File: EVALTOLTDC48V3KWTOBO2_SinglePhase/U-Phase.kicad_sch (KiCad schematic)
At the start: 35 parts, among them Q1 IAUS300N10S5N015TATMA1, Q4 IAUS300N10S5N015TATMA1, U3 2EDL8x24G, U4 NL27WZ08USG

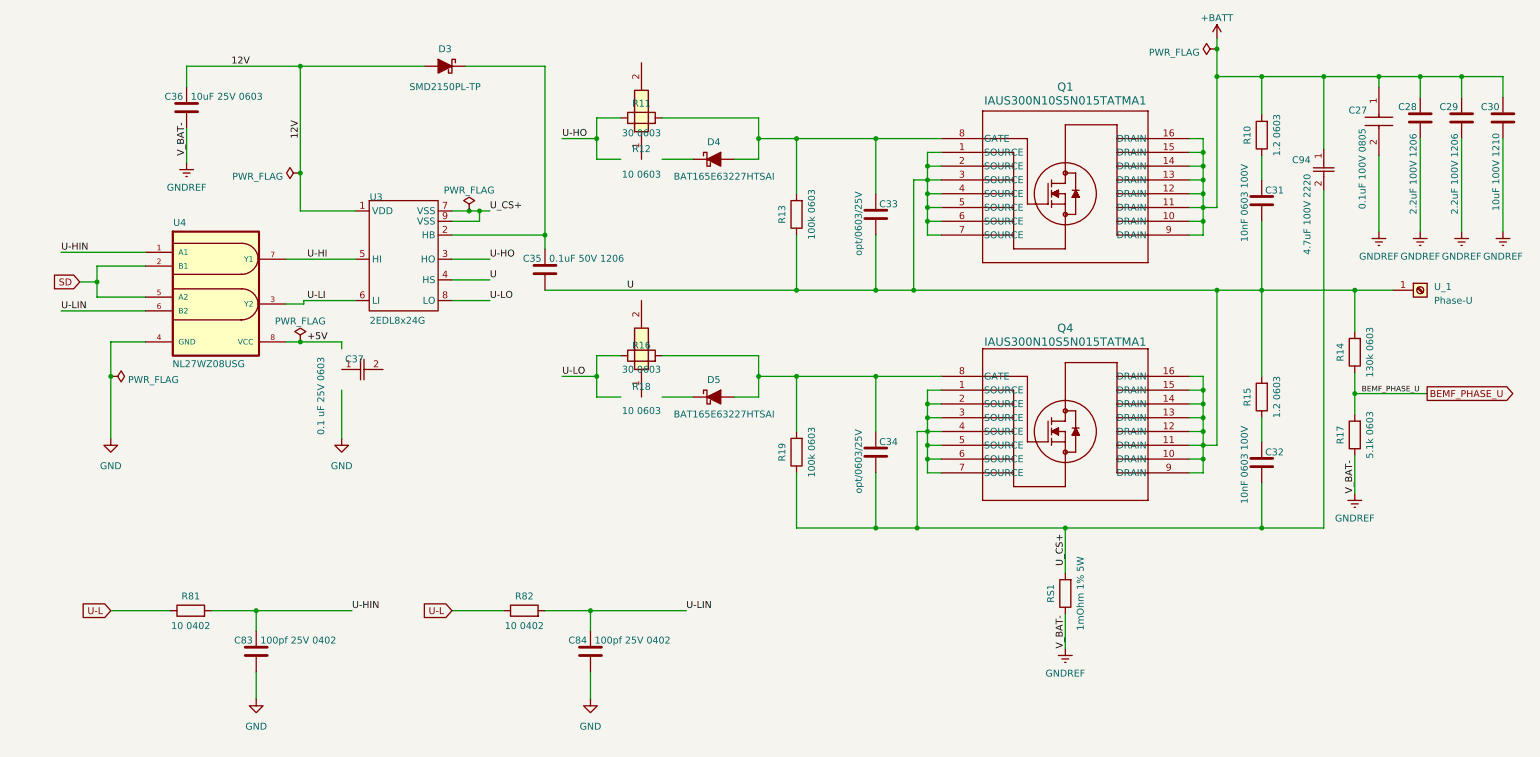
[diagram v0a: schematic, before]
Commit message: Change 1
Changed DC-DC Buck Converter and U Phase
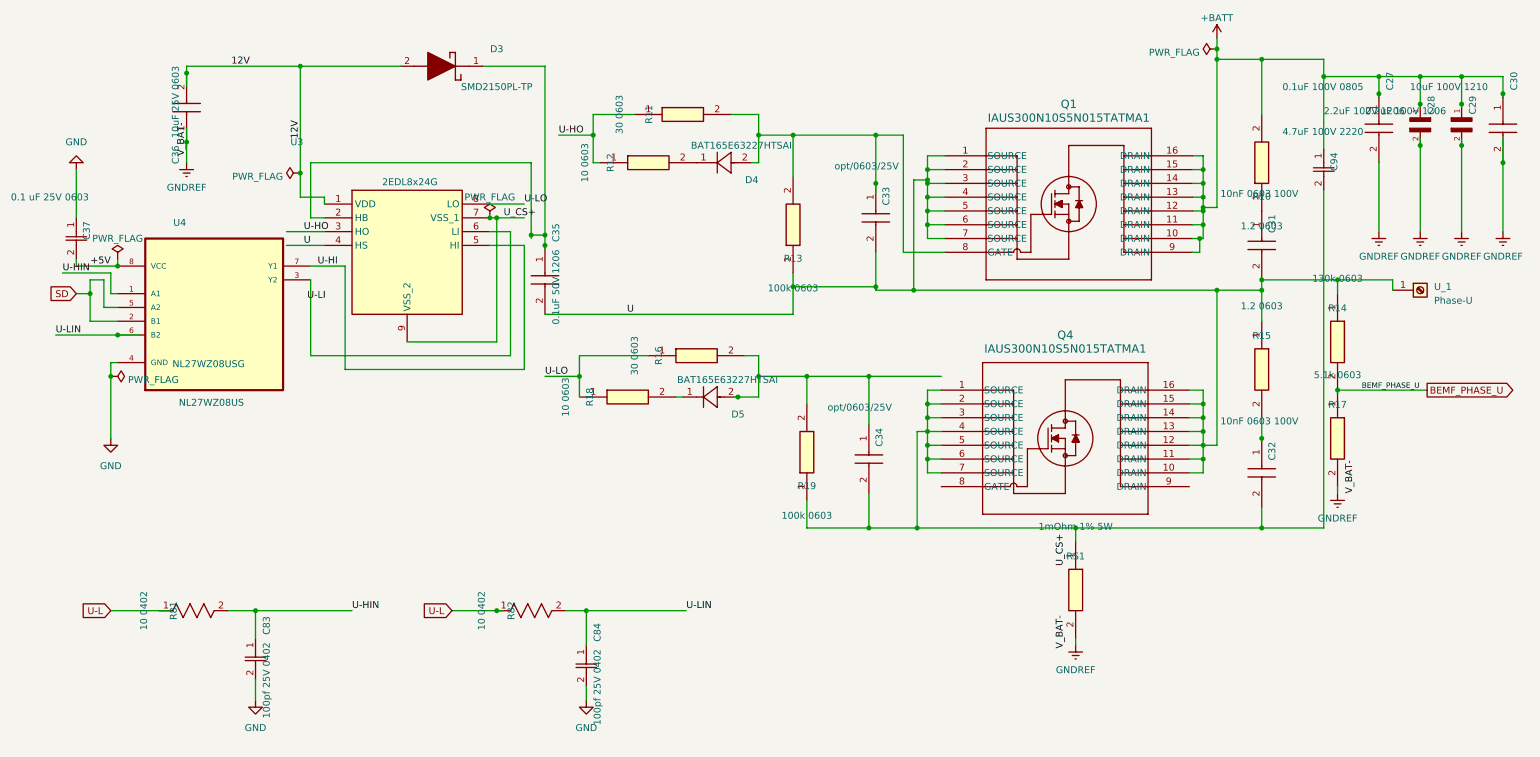
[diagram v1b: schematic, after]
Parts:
- C27: footprint just-footprints:C0805 -> Footprints .mod:C27; symbol C0805X104K1RAC3316:C0805X104K1RAC3316 -> C27:C0805X104K1RAC3316
- C28: footprint (none) -> Footprints .mod:C28; symbol Device:C -> C28:GCM31CC72A225KE02L
- C29: footprint (none) -> Footprints .mod:C29; symbol Device:C -> C29:GCM31CC72A225KE02L
- C30: footprint (none) -> Footprints .mod:C30; symbol Device:C -> C30:CL32Y106KCVZNWE; Arrow Part Number (none) -> CL32Y106KCVZNWE; Arrow Price/Stock (none) -> https://www.arrow.com/en/products/cl32y106kcvznwe/samsung-e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; Height (none) -> 2.8; Manufacturer_Name (none) -> SAMSUNG; Manufacturer_Part_Number (none) -> CL32Y106KCVZNWE; Mouser Part Number (none) -> 187-CL32Y106KCVZNWE; Mouser Price/Stock (none) -> https://www.mouser.co.uk/ProductDetail/Samsung-Electro-Mech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
- C31: footprint (none) -> Footprints .mod:C31; symbol Device:C -> C31:CL10B103KC8WPJL; Height (none) -> 0.9; Manufacturer_Name (none) -> SAMSUNG; Manufacturer_Part_Number (none) -> CL10B103KC8WPJL
- C32: footprint (none) -> Footprints .mod:C32; symbol Device:C -> C32:CL10B103KC8WPJL; Height (none) -> 0.9; Manufacturer_Name (none) -> SAMSUNG; Manufacturer_Part_Number (none) -> CL10B103KC8WPJL
- C33: footprint (none) -> Footprints .mod:C33; symbol Device:C -> C33:GRM188R61E106MA73J; Height (none) -> 0.9; Manufacturer_Name (none) -> Murata Electronics; Manufacturer_Part_Number (none) -> GRM188R61E106MA73J; Mouser Part Number (none) -> 81-GRM188R61E106MA3J; Mouser Price/Stock (none) -> https://www.mouser.co.uk/ProductDetail/Murata-Electronics/G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
- C34: footprint (none) -> Footprints .mod:C34; symbol Device:C -> C34:GRM188R61E106MA73J; Height (none) -> 0.9; Manufacturer_Name (none) -> Murata Electronics; Manufacturer_Part_Number (none) -> GRM188R61E106MA73J; Mouser Part Number (none) -> 81-GRM188R61E106MA3J; Mouser Price/Stock (none) -> https://www.mouser.co.uk/ProductDetail/Murata-Electronics/G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
- C35: footprint (none) -> Footprints .mod:C35; symbol Device:C -> C35:C1206F104K5RACAUTO; Manufacturer_Name (none) -> KEMET; Manufacturer_Part_Number (none) -> C1206F104K5RACAUTO; Mouser Part Number (none) -> 80-C1206F104K5RAUTO; Mouser Price/Stock (none) -> https://www.mouser.co.uk/ProductDetail/KEMET/C1206F104K5RAC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
- C36: footprint (none) -> Footprints .mod:C36; symbol Device:C -> C36:GRM188R61E106MA73J; Height (none) -> 0.9; Manufacturer_Name (none) -> Murata Electronics; Manufacturer_Part_Number (none) -> GRM188R61E106MA73J; Mouser Part Number (none) -> 81-GRM188R61E106MA3J; Mouser Price/Stock (none) -> https://www.mouser.co.uk/ProductDetail/Murata-Electronics/G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
- C37: footprint just-footprints:CAPC17795_95N_KEM -> Footprints .mod:C37; symbol C0603X104M3RAUTO:C0603X104M3RACTU -> C37:C0603X104M3RACTU
- C83: footprint (none) -> Footprints .mod:C83; symbol Device:C -> C83:C0402C101K3RACTU
- C84: footprint (none) -> Footprints .mod:C84; symbol Device:C -> C84:C0402C101K3RACTU
- C94: footprint just-footprints:CAPC220145_88N_KEM -> Footprints .mod:C94; symbol C0805X475K3RAC7800:C0805C681J5RACTU -> C94:22201C475KAT2A
- D3: symbol Device:D_Schottky_Filled -> D3:SMD2150PL-TP; Height (none) -> 1.35; Manufacturer_Name (none) -> MCC; Manufacturer_Part_Number (none) -> SMD2150PL-TP; Mouser Part Number (none) -> 833-SMD2150PL-TP; Mouser Price/Stock (none) -> https://www.mouser.co.uk/ProductDetail/Micro-Commercial-Com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
- D4: symbol Device:D_Schottky_Filled -> D4:BAT165E6327HTSA1
- D5: symbol Device:D_Schottky_Filled -> D5:BAT165E6327HTSA1
- Q1: footprint just-footprints:PG-HDSOP-16-2 -> Footprints .mod:Q1; symbol IAUS300N10S5N015T:IAUS300N10S5N015TATMA1 -> Q1:IPTC015N10NM5ATMA1
- Q4: footprint just-footprints:PG-HDSOP-16-2 -> Footprints .mod:Q4; symbol IAUS300N10S5N015T:IAUS300N10S5N015TATMA1 -> Q4:IPTC015N10NM5ATMA1
- R10: footprint (none) -> Footprints .mod:R10; symbol Device:R -> R10:CRCW060330R0JNEA; Arrow Part Number (none) -> CRCW060330R0JNEA; Height (none) -> 0.5; Manufacturer_Name (none) -> Vishay; Manufacturer_Part_Number (none) -> CRCW060330R0JNEA
- R11: footprint (none) -> Footprints .mod:R11; symbol Device:R -> R11:CRCW060330R0JNEA; Arrow Part Number (none) -> CRCW060330R0JNEA; Height (none) -> 0.5; Manufacturer_Name (none) -> Vishay; Manufacturer_Part_Number (none) -> CRCW060330R0JNEA
- R12: footprint ERJP03_PA3_(0603) -> Footprints .mod:R12; symbol ERJ-PA3J100V:ERJ-PA3J100V -> R12:ERJ-PA3J100V
- R13: footprint (none) -> Footprints .mod:R13; symbol Device:R -> R13:RCA0603100KFKEAHP; Arrow Part Number (none) -> RCA0603100KFKEAHP; Arrow Price/Stock (none) -> https://www.arrow.com/en/products/rca0603100kfkeahp/vishay?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; Height (none) -> 0.55; Manufacturer_Name (none) -> Vishay; Manufacturer_Part_Number (none) -> RCA0603100KFKEAHP; Mouser Part Number (none) -> 71-RCA0603100KFKEAHP; Mouser Price/Stock (none) -> https://www.mouser.co.uk/ProductDetail/Vishay-Draloric/RCA0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
- R14: footprint (none) -> Footprints .mod:R14; symbol Device:R -> R14:RCA0603100KFKEAHP; Arrow Part Number (none) -> RCA0603100KFKEAHP; Arrow Price/Stock (none) -> https://www.arrow.com/en/products/rca0603100kfkeahp/vishay?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; Height (none) -> 0.55; Manufacturer_Name (none) -> Vishay; Manufacturer_Part_Number (none) -> RCA0603100KFKEAHP; Mouser Part Number (none) -> 71-RCA0603100KFKEAHP; Mouser Price/Stock (none) -> https://www.mouser.co.uk/ProductDetail/Vishay-Draloric/RCA0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
- R15: footprint (none) -> Footprints .mod:R15; symbol Device:R -> R15:CRCW060330R0JNEA; Arrow Part Number (none) -> CRCW060330R0JNEA; Height (none) -> 0.5; Manufacturer_Name (none) -> Vishay; Manufacturer_Part_Number (none) -> CRCW060330R0JNEA
- R16: footprint (none) -> Footprints .mod:R16; symbol Device:R -> R16:CRCW060330R0JNEA; Arrow Part Number (none) -> CRCW060330R0JNEA; Height (none) -> 0.5; Manufacturer_Name (none) -> Vishay; Manufacturer_Part_Number (none) -> CRCW060330R0JNEA
- R17: footprint (none) -> Footprints .mod:R17; symbol Device:R -> R17:RCS06035K10FKEA; Manufacturer_Name (none) -> Vishay; Manufacturer_Part_Number (none) -> RCS06035K10FKEA; Mouser Part Number (none) -> 71-RCS06035K10FKEA; Mouser Price/Stock (none) -> https://www.mouser.com/Search/Refine.aspx?Keyword=71-RCS060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
- R18: footprint ERJP03_PA3_(0603) -> Footprints .mod:R18; symbol ERJ-PA3J100V:ERJ-PA3J100V -> R18:ERJ-PA3J100V
- R19: footprint (none) -> Footprints .mod:R19; symbol Device:R -> R19:RCA0603100KFKEAHP; Arrow Part Number (none) -> RCA0603100KFKEAHP; Arrow Price/Stock (none) -> https://www.arrow.com/en/products/rca0603100kfkeahp/vishay?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; Height (none) -> 0.55; Manufacturer_Name (none) -> Vishay; Manufacturer_Part_Number (none) -> RCA0603100KFKEAHP; Mouser Part Number (none) -> 71-RCA0603100KFKEAHP; Mouser Price/Stock (none) -> https://www.mouser.co.uk/ProductDetail/Vishay-Draloric/RCA0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
- R81: footprint (none) -> Footprints .mod:R81; symbol Device:R -> R81:CRGP0402F10R
- R82: footprint (none) -> Footprints .mod:R82; symbol Device:R -> R82:CRGP0402F10R
- RS1: symbol Device:R -> R51:ERJ-PA3J100V; Height (none) -> 0.55; Manufacturer_Name (none) -> Panasonic; Manufacturer_Part_Number (none) -> ERJ-PA3J100V; Mouser Part Number (none) -> 667-ERJ-PA3J100V; Mouser Price/Stock (none) -> https://www.mouser.co.uk/ProductDetail/Panasonic/ERJ-PA3J10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
- U3: footprint (none) -> Footprints .mod:U3; symbol 2EDL8124G:2EDL8124G -> U3:2EDL8124GXUMA1; Height (none) -> 1; Manufacturer_Name (none) -> Infineon; Manufacturer_Part_Number (none) -> 2EDL8124GXUMA1
- U4: footprint NL27WZ08USG:SOP50P310X90-8N -> Footprints .mod:U4; symbol NL27WZ08USG:NL27WZ08USG -> U4:NL27WZ08USG; Description_1 (none) -> AND Gate 2-Element 2-IN CMOS 8-Pin US T/R
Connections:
- net +5V: now also C37.2
- net 12V: now also C36.2; no longer C36.1
- net BEMF_PHASE_U: now also R14.2, R17.1; no longer R14.1, R17.2
- net GND: now also C37.1
- net GNDREF: now also C36.1, R17.2, RS1.2; no longer C36.2, R17.1, RS1.1
- net U: now also R14.1, R15.1; no longer Q4.9 (DRAIN), R14.2, R15.2
- net U-HO: now also R12.1
- net U-L: no longer R81.1
- net U-LI: no longer U3.6 (LI), U4.3 (Y2)
- net U-LO: now also R18.1
- net U_CS+: no longer C32.2, C34.2, C94.2, Q4.1 (SOURCE), Q4.2 (SOURCE), Q4.3 (SOURCE), Q4.4 (SOURCE), Q4.5 (SOURCE), Q4.6 (SOURCE), Q4.7 (SOURCE), R19.1, RS1.2
- net at C34.1, D5.2, R16.2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: no longer Q4.8 (GATE)
- net at C32.1: now also R15.2; no longer R15.1
- net at D5.1: now also R18.2
- net at R12.2: now also D4.1
- new net: C32.2, C34.2, C94.2, Q4.1 (SOURCE), Q4.2 (SOURCE), Q4.3 (SOURCE), Q4.4 (SOURCE), Q4.5 (SOURCE), Q4.6 (SOURCE), Q4.7 (SOURCE), R19.1, RS1.1
- new net: U3.6 (LI), U4.3 (Y2)
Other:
- note added: "NL27WZ08US"
- moved on the sheet: C27, C37, R12, R18
